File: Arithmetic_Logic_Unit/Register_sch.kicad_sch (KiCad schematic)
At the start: 19 parts, among them IC1 SN54173J, IC2 SN54173J, U1 74LS245

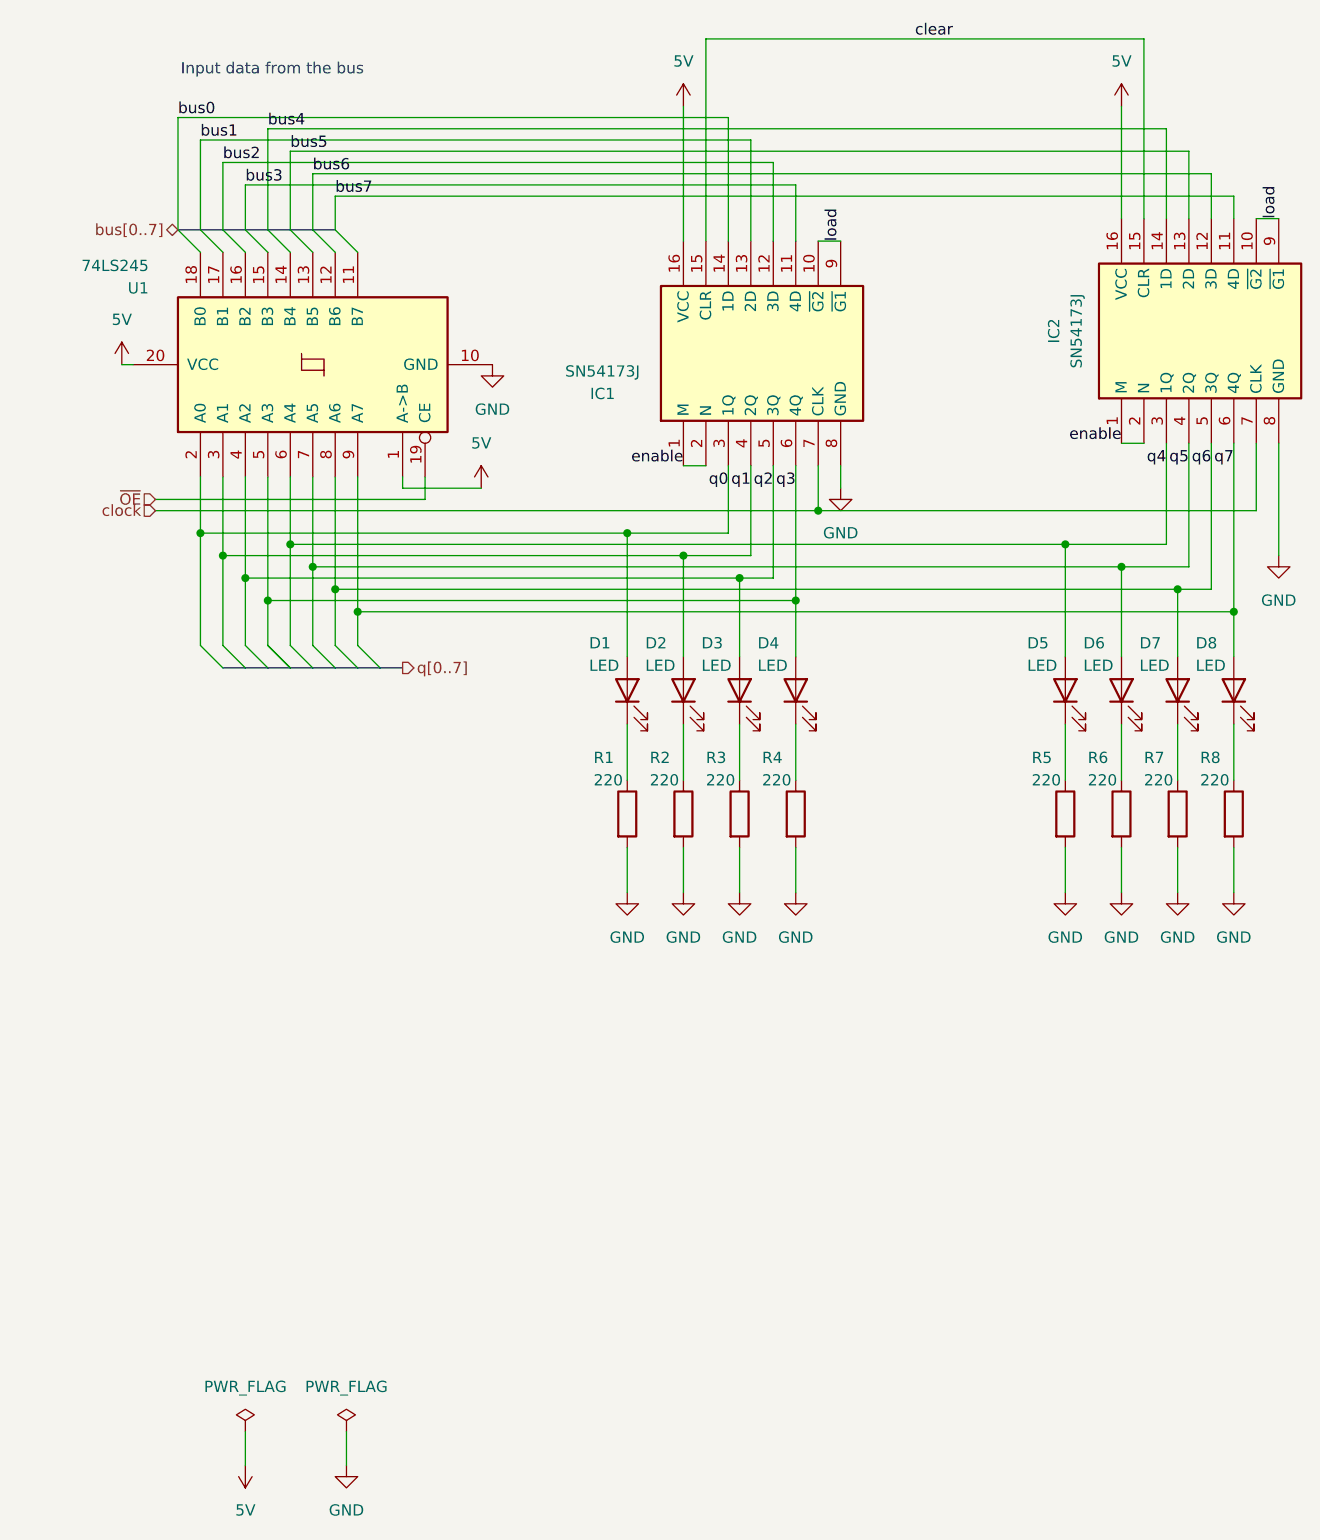
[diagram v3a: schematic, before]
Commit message: removed buses and replaced with hierarchical labels
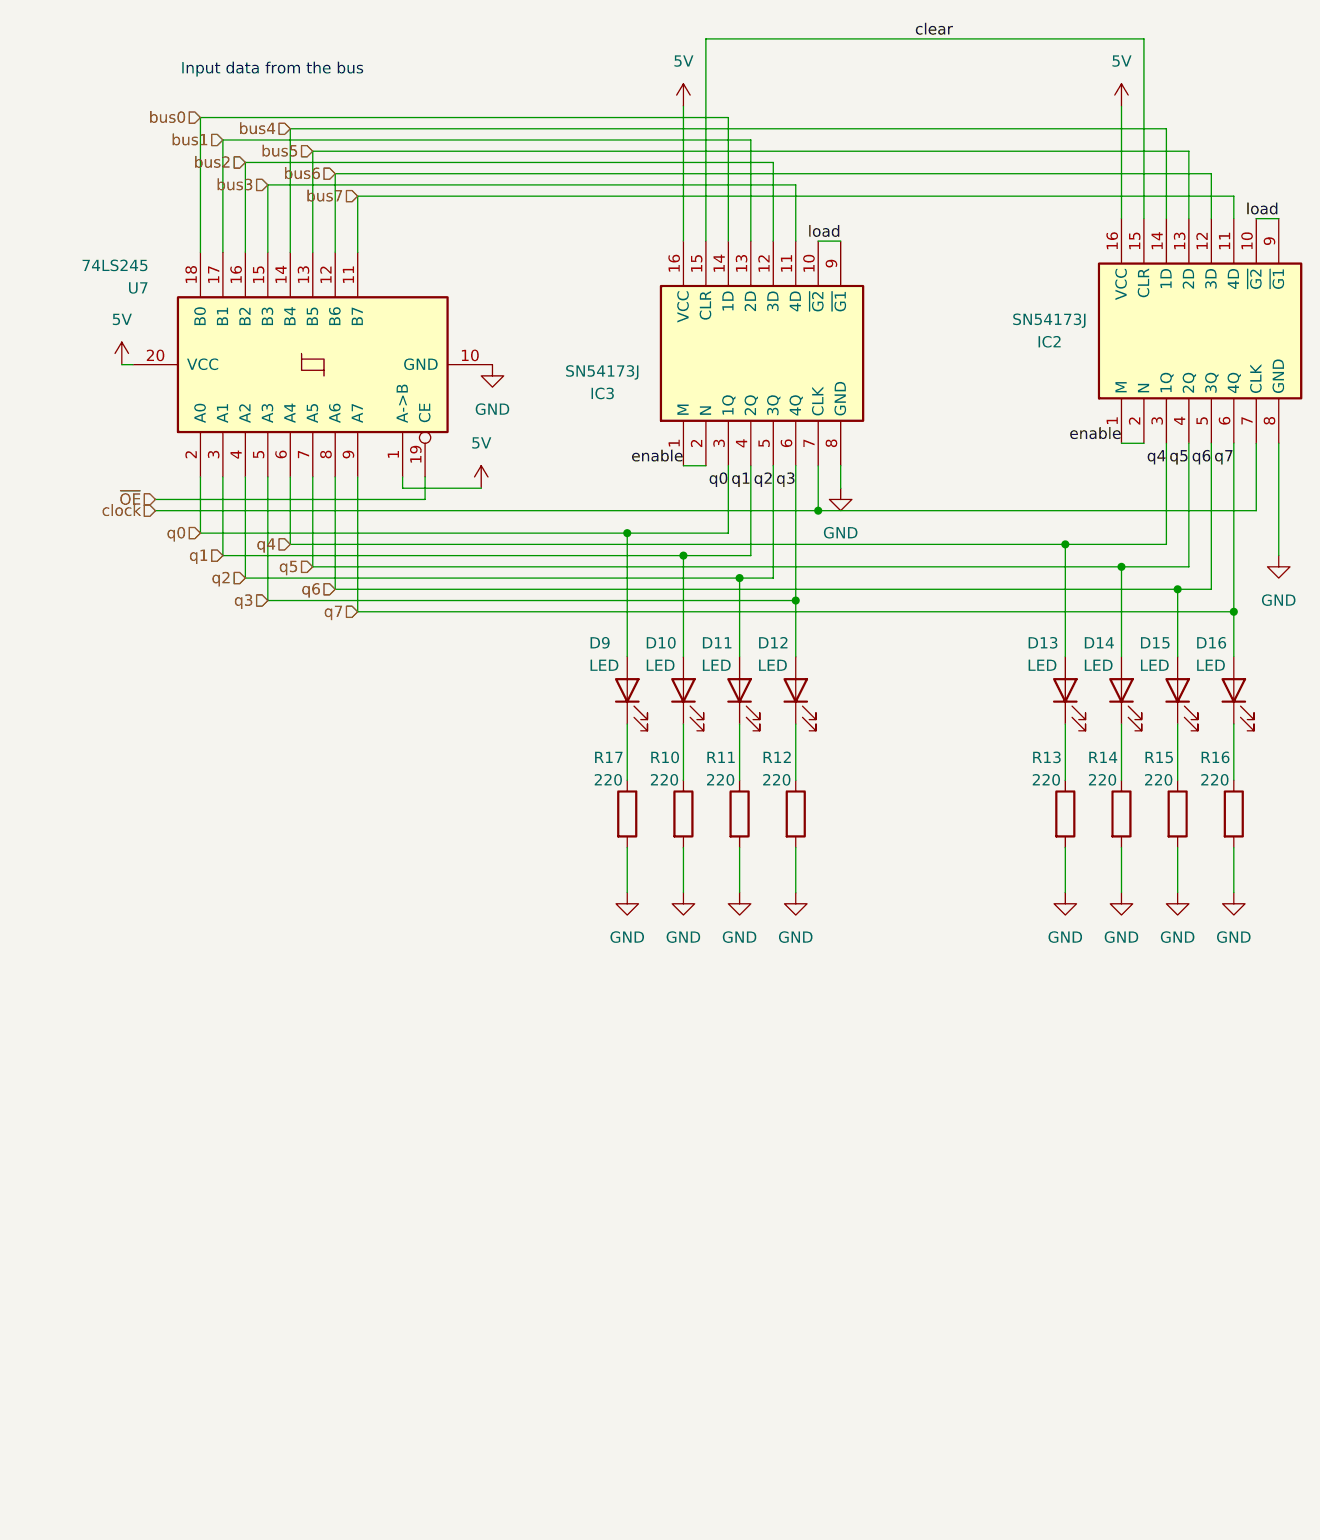
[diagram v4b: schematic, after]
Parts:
- renumbered D2 to D10, D3 to D11, D4 to D12, D5 to D13, D6 to D14, D7 to D15, D8 to D16, D1 to D9, IC1 to IC3, R2 to R10, R3 to R11, R4 to R12, R5 to R13, R6 to R14, R7 to R15, R8 to R16, R1 to R17, U1 to U7
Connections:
- net bus[0..7] is gone; now on net bus0: IC3.14 (1D)
- net bus1: now also U7.17 (B1)
- net bus2: now also U7.16 (B2)
- net bus3: now also U7.15 (B3)
- net bus4: now also U7.14 (B4)
- net bus5: now also U7.13 (B5)
- net bus6: now also U7.12 (B6)
- net bus7: now also U7.11 (B7)
- net bus0: now reaches U7.18 (B0)
